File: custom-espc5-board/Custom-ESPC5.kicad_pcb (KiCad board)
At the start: 4 copper layers, 64.8 x 57 mm, 47 parts, among them J1 Screw_Terminal_01x02, J10 Barrel_Jack, J12 Conn_01x05, J13 Conn_01x05, J2 Conn_01x03, J3 Conn_01x03, J4 USB_C_Receptacle_USB2.0_14P, J5 Conn_01x03, J6 Screw_Terminal_01x03, SW1 SW_Nidec_CAS-120A1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

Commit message: idk
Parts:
- moved ? 1.11 mm to (52.5, 133.1)
- moved ? 1.11 mm to (52.6, 83.8)
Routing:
- net /A1: vias 1 -> 0
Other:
- board size 64.8 x 57 mm -> 64 x 57 mm
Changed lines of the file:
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@@
 	(footprint ""
 		(layer "F.Cu")
-		(at 51.4 133.25)
+		(at 52.5 133.1)
 		(property "Reference" ""
 			(at 0 0 0)
@@
 	(footprint ""
 		(layer "F.Cu")
-		(at 51.55 83.9)
+		(at 52.65 83.75)
 		(property "Reference" ""
 			(at 0 0 0)
@@
 	)
 	(gr_rect
-		(start 47.8 80.1)
+		(start 48.6 80.1)
 		(end 112.6 137.1)
 		(stroke
@@
 		(net 22)
 	)
-	(via
-		(at 65.45 105.65)
-		(size 0.6)
-		(drill 0.3)
-		(layers "F.Cu" "B.Cu")
-		(net 22)
-	)
 	(segment
 		(start 82.66 98.04)
@@
 		(width 0.2)
 		(layer "F.Cu")
-		(net 27)
-	)
-	(segment
-		(start 105.65 113.55)
-		(end 105.475 113.725)
-		(width 0.2)
-		(layer "F.Cu")

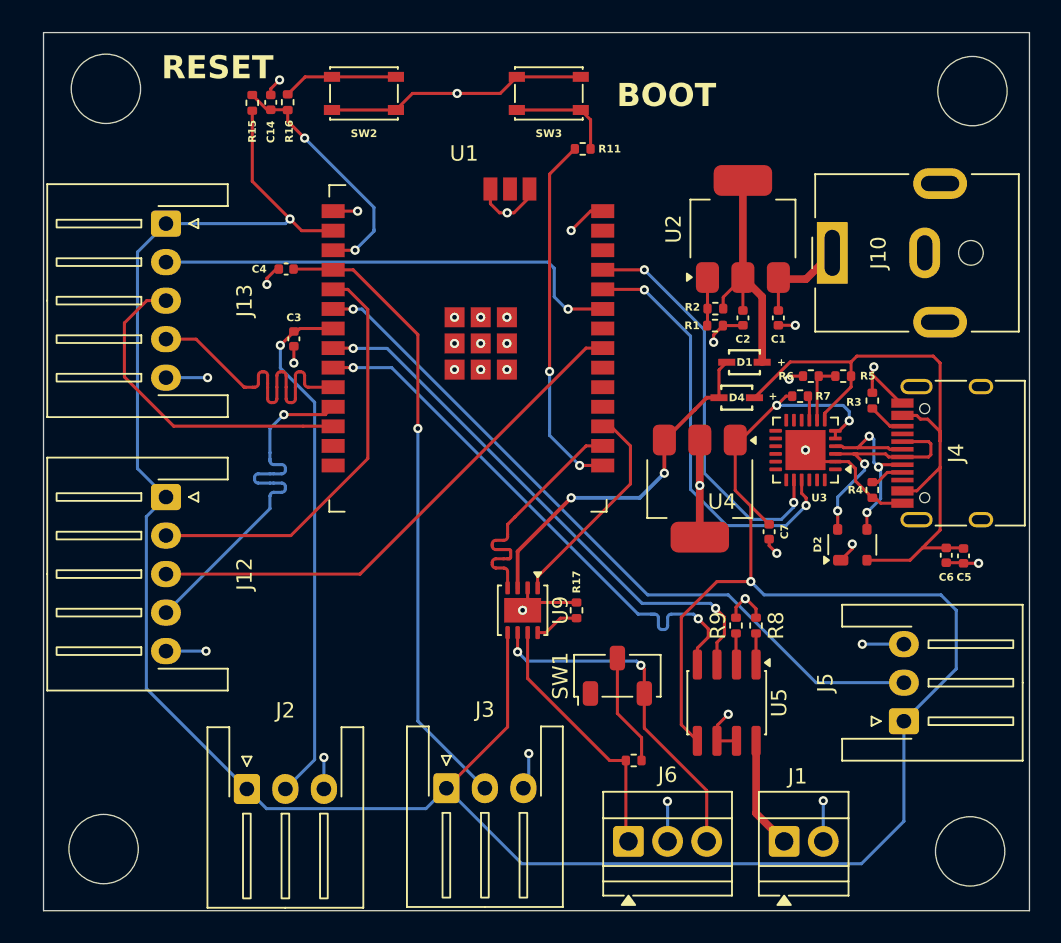
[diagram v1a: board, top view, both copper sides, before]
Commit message: fix some silkscreens, get rounded corners
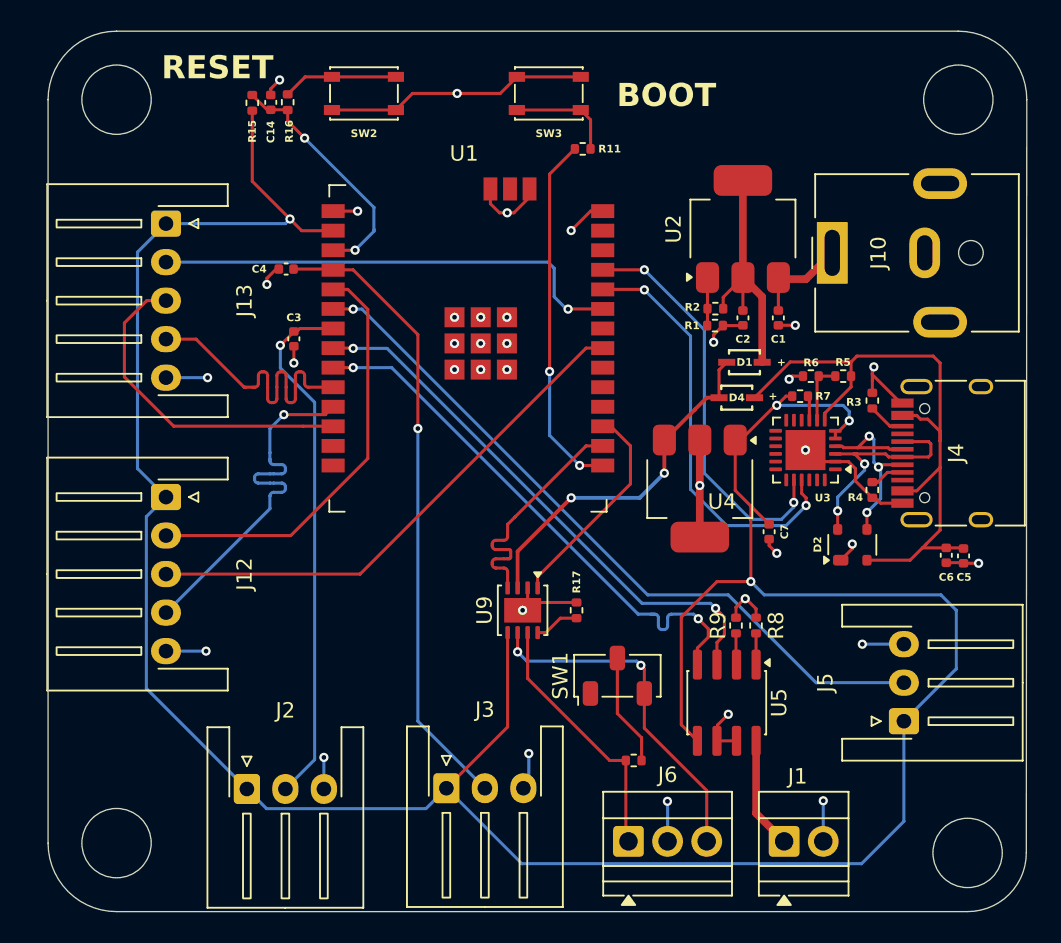
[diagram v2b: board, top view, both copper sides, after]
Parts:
- removed the ? at (52.5, 133.1)
- removed the ? at (52.6, 83.8)
- removed the ? at (108.9, 83.9)
- added ?: , , F.Cu at (108.0, 84.5)
- added ?: , , F.Cu at (53.3, 132.7)
- added ?: , , F.Cu at (53.3, 84.5)
- moved ? 0.19 mm to (108.6, 133.3)
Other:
- board size 64 x 57 mm -> 63.5 x 57.1 mm
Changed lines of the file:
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@@
 		)
 	)
-	(footprint ""
-		(layer "F.Cu")
-		(at 52.5 133.1)
-		(property "Reference" ""
-			(at 0 0 0)
-			(layer "F.SilkS")
-			(effects
-				(font
-					(size 1.27 1.27)
-					(thickness 0.15)
-				)
-			)
-		)
-		(property "Value" ""
-			(at 0 0 0)
-			(layer "F.Fab")
-			(effects
-				(font
-					(size 1.27 1.27)
-					(thickness 0.15)
-				)
-			)
-		)
-		(property "Datasheet" ""
-			(at 0 0 0)
-			(layer "F.Fab")
-			(hide yes)
-			(effects
-				(font
-					(size 1.27 1.27)
-					(thickness 0.15)
-				)
-			)
-		)
-		(property "Description" ""
-			(at 0 0 0)
-			(layer "F.Fab")
-			(hide yes)
-			(effects
-				(font
-					(size 1.27 1.27)
-					(thickness 0.15)
-				)
-			)
-		)
-		(pad "" np_thru_hole circle
-			(at 0 0)
-			(size 4.5 4.5)
-			(drill 4.5)
-			(layers "*.Cu" "*.Mask")
-		)
-		(embedded_fonts no)
-	)
 	(footprint "Resistor_SMD:R_0402_1005Metric"
 		(layer "F.Cu")
@@
 		(tags "resistor")
 		(property "Reference" "R4"
-			(at 0 1.1 180)
+			(at 0.485 1.1 180)
 			(layer "F.SilkS")
 			(effects
@@
 		(tags "HVSON NoLead")
 		(property "Reference" "U9"
-			(at 0 -2.45 90)
+			(at 0 2.475 90)
 			(layer "F.SilkS")
 			(effects
@@
 		)
 	)
+	(footprint ""
+		(layer "F.Cu")
+		(at 107.98191 84.455)
+		(property "Reference" ""
+			(at 0 0 0)
+			(layer "F.SilkS")
+			(effects
+				(font
+					(size 1.27 1.27)
+					(thickness 0.15)
+				)
+			)
+		)
+		(property "Value" ""
+			(at 0 0 0)
+			(layer "F.Fab")
+			(effects
+				(font
+					(size 1.27 1.27)
+					(thickness 0.15)
+				)
+			)
+		)
+		(property "Datasheet" ""
+			(at 0 0 0)
+			(layer "F.Fab")
+			(hide yes)
+			(effects
+				(font
+					(size 1.27 1.27)
+					(thickness 0.15)
+				)
+			)
+		)
+		(property "Description" ""
+			(at 0 0 0)
+			(layer "F.Fab")
+			(hide yes)
+			(effects
+				(font
+					(size 1.27 1.27)
+					(thickness 0.15)
+				)
+			)
+		)
+		(pad "" np_thru_hole circle
+			(at 0 0)
+			(size 4.5 4.5)
+			(drill 4.5)
+			(layers "*.Cu" "*.Mask")
+		)
+		(embedded_fonts no)
+	)
 	(footprint "Resistor_SMD:R_0402_1005Metric"
 		(layer "F.Cu")
@@
 		)
 	)
-	(footprint ""
-		(layer "F.Cu")
-		(at 52.65 83.75)
-		(property "Reference" ""
-			(at 0 0 0)
-			(layer "F.SilkS")
-			(effects
-				(font
-					(size 1.27 1.27)
-					(thickness 0.15)
-				)
-			)
-		)
-		(property "Value" ""
-			(at 0 0 0)
-			(layer "F.Fab")
-			(effects
-				(font
-					(size 1.27 1.27)
-					(thickness 0.15)
-				)
-			)
-		)
-		(property "Datasheet" ""
-			(at 0 0 0)
-			(layer "F.Fab")
-			(hide yes)
-			(effects
-				(font
-					(size 1.27 1.27)
-					(thickness 0.15)
-				)
-			)
-		)
-		(property "Description" ""
-			(at 0 0 0)
-			(layer "F.Fab")
-			(hide yes)
-			(effects
-				(font
-					(size 1.27 1.27)
-					(thickness 0.15)
-				)
-			)
-		)
-		(pad "" np_thru_hole circle
-			(at 0 0)
-			(size 4.5 4.5)
-			(drill 4.5)
-			(layers "*.Cu" "*.Mask")
-		)
-		(embedded_fonts no)
-	)
 	(footprint "Resistor_SMD:R_0402_1005Metric"
 		(layer "F.Cu")
@@
 		(tags "resistor")
 		(property "Reference" "R6"
-			(at 1.61 0 0)
+			(at -0.015 0.875 0)
 			(layer "F.SilkS")
 			(effects
@@
 		(tags "resistor")
 		(property "Reference" "R5"
-			(at -1.59 0.01 0)
+			(at 0.01 0.9 0)
 			(layer "F.SilkS")
 			(effects
@@
 	(footprint ""
 		(layer "F.Cu")
-		(at 108.9 83.9)
+		(at 53.34 132.715)
 		(property "Reference" ""
 			(at 0 0 0)
@@
 	(footprint ""
 		(layer "F.Cu")
-		(at 108.75 133.25)
+		(at 53.34 84.455)
+		(property "Reference" ""
+			(at 0 0 0)
+			(layer "F.SilkS")
+			(effects
+				(font
+					(size 1.27 1.27)
+					(thickness 0.15)
+				)
+			)
+		)
+		(property "Value" ""
+			(at 0 0 0)
+			(layer "F.Fab")
+			(effects
+				(font
+					(size 1.27 1.27)
+					(thickness 0.15)
+				)
+			)
+		)
+		(property "Datasheet" ""
+			(at 0 0 0)
+			(layer "F.Fab")
+			(hide yes)
+			(effects
+				(font
+					(size 1.27 1.27)
+					(thickness 0.15)
+				)
+			)
+		)
+		(property "Description" ""
+			(at 0 0 0)
+			(layer "F.Fab")
+			(hide yes)
+			(effects
+				(font
+					(size 1.27 1.27)
+					(thickness 0.15)
+				)
+			)
+		)
+		(pad "" np_thru_hole circle
+			(at 0 0)
+			(size 4.5 4.5)
+			(drill 4.5)
+			(layers "*.Cu" "*.Mask")
+		)
+		(embedded_fonts no)
+	)
+	(footprint ""
+		(layer "F.Cu")
+		(at 108.585 133.35)
 		(property "Reference" ""
 			(at 0 0 0)
@@
 		(tags "QFN NoLead")
 		(property "Reference" "U3"
-			(at -0.8875 -3.1 0)
+			(at -1.1125 -3.1 0)
 			(layer "F.SilkS")
 			(effects
@@
 		)
 	)
-	(gr_rect
-		(start 48.6 80.1)
-		(end 112.6 137.1)
+	(gr_line
+		(start 112.42691 84.455)
+		(end 112.395 133.35)
+		(stroke
+			(width 0.05)
+			(type default)
+		)
+		(layer "Edge.Cuts")
+	)
+	(gr_arc
+		(start 112.395 133.35)
+		(mid 111.279077 136.044077)
+		(end 108.585 137.16)
+		(stroke
+			(width 0.05)
+			(type default)
+		)
+		(layer "Edge.Cuts")
+	)
+	(gr_line
+		(start 107.9819 80.01)
+		(end 53.34 80.01)
+		(stroke
+			(width 0.05)
+			(type default)
+		)
+		(layer "Edge.Cuts")
+	)
+	(gr_line
+		(start 48.895 84.455)
+		(end 48.895 132.715)
+		(stroke
+			(width 0.05)
+			(type default)
+		)
+		(layer "Edge.Cuts")
+	)
+	(gr_arc
+		(start 107.98191 80.01)
+		(mid 111.125 81.31191)
+		(end 112.42691 84.455)
+		(stroke
+			(width 0.05)
+			(type default)
+		)
+		(layer "Edge.Cuts")
+	)
+	(gr_line
+		(start 53.34 137.16)
+		(end 108.585 137.16)
+		(stroke
+			(width 0.05)
+			(type default)
+		)
+		(layer "Edge.Cuts")
+	)
+	(gr_arc
+		(start 48.895 84.455)
+		(mid 50.19691 81.31191)
+		(end 53.34 80.01)
+		(stroke
+			(width 0.05)
+			(type default)
+		)
+		(layer "Edge.Cuts")
+	)
+	(gr_arc
+		(start 53.34 137.16)
+		(mid 50.19691 135.85809)
+		(end 48.895 132.715)
 		(stroke
 			(width 0.05)
-			(type solid)
+			(type default)
 		)
-		(fill no)
 		(layer "Edge.Cuts")
 	)
